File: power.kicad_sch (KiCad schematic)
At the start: 58 parts, among them Q1 AO3415A, SW2 SW_Push_Dual, U1 BQ25619RTWR, U2 TPS22917DBVR, U3 TPS63802DLAR, U4 MAX17260SEWL

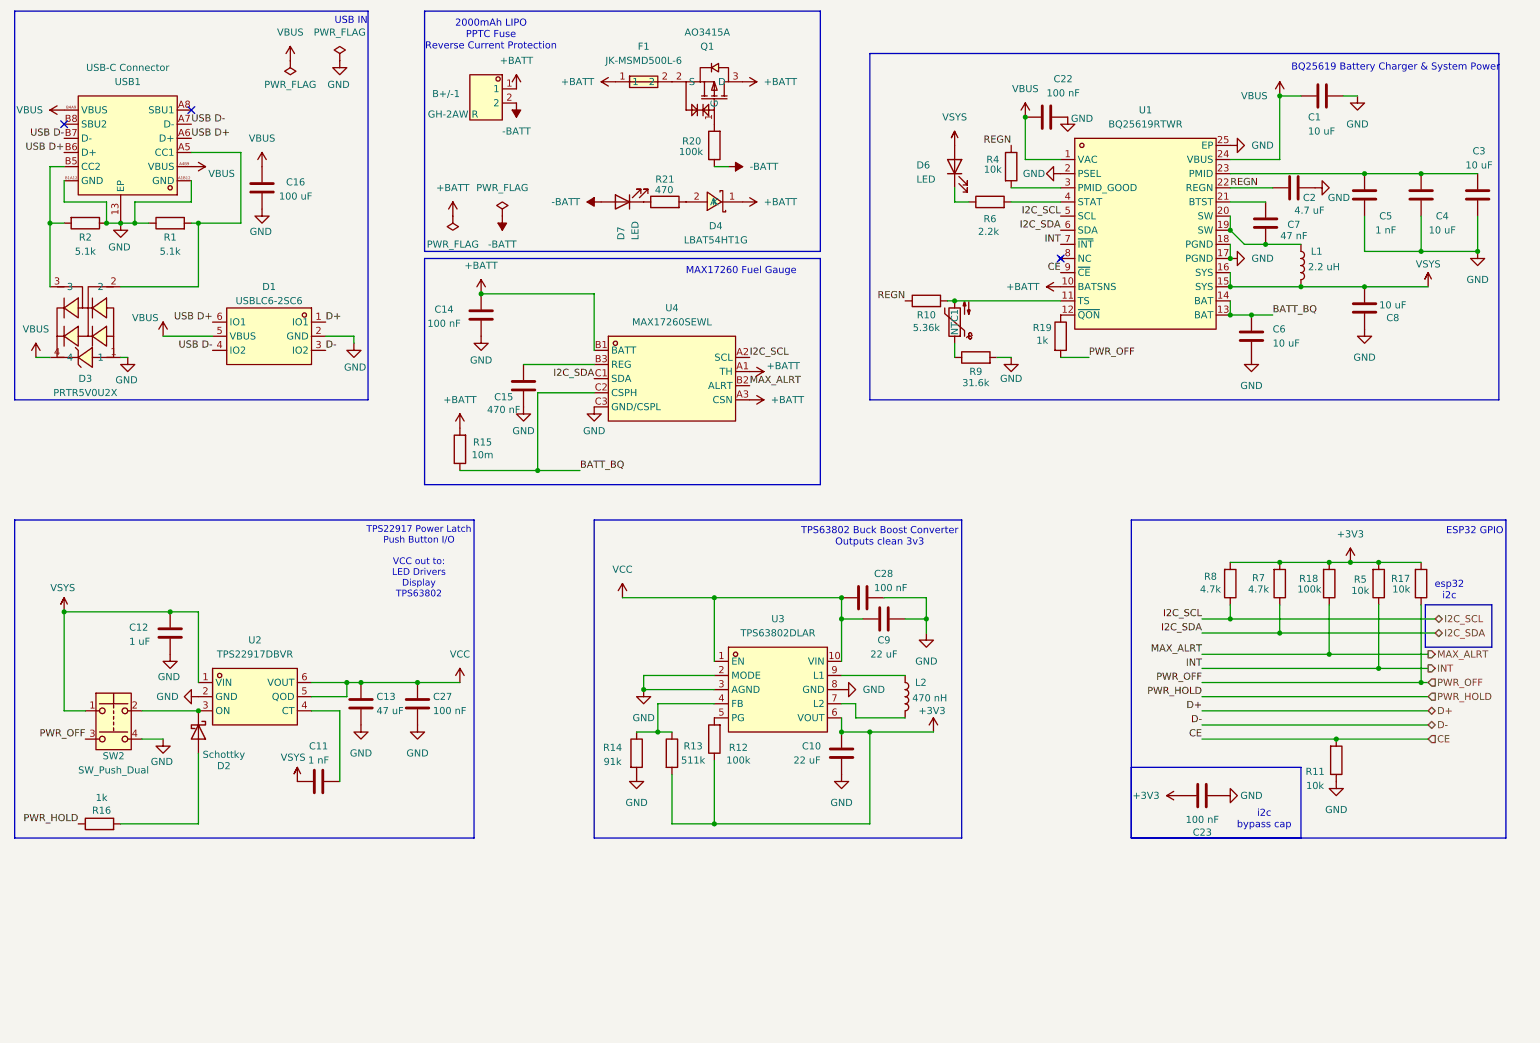
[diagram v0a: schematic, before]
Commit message: Add test points to schematic.
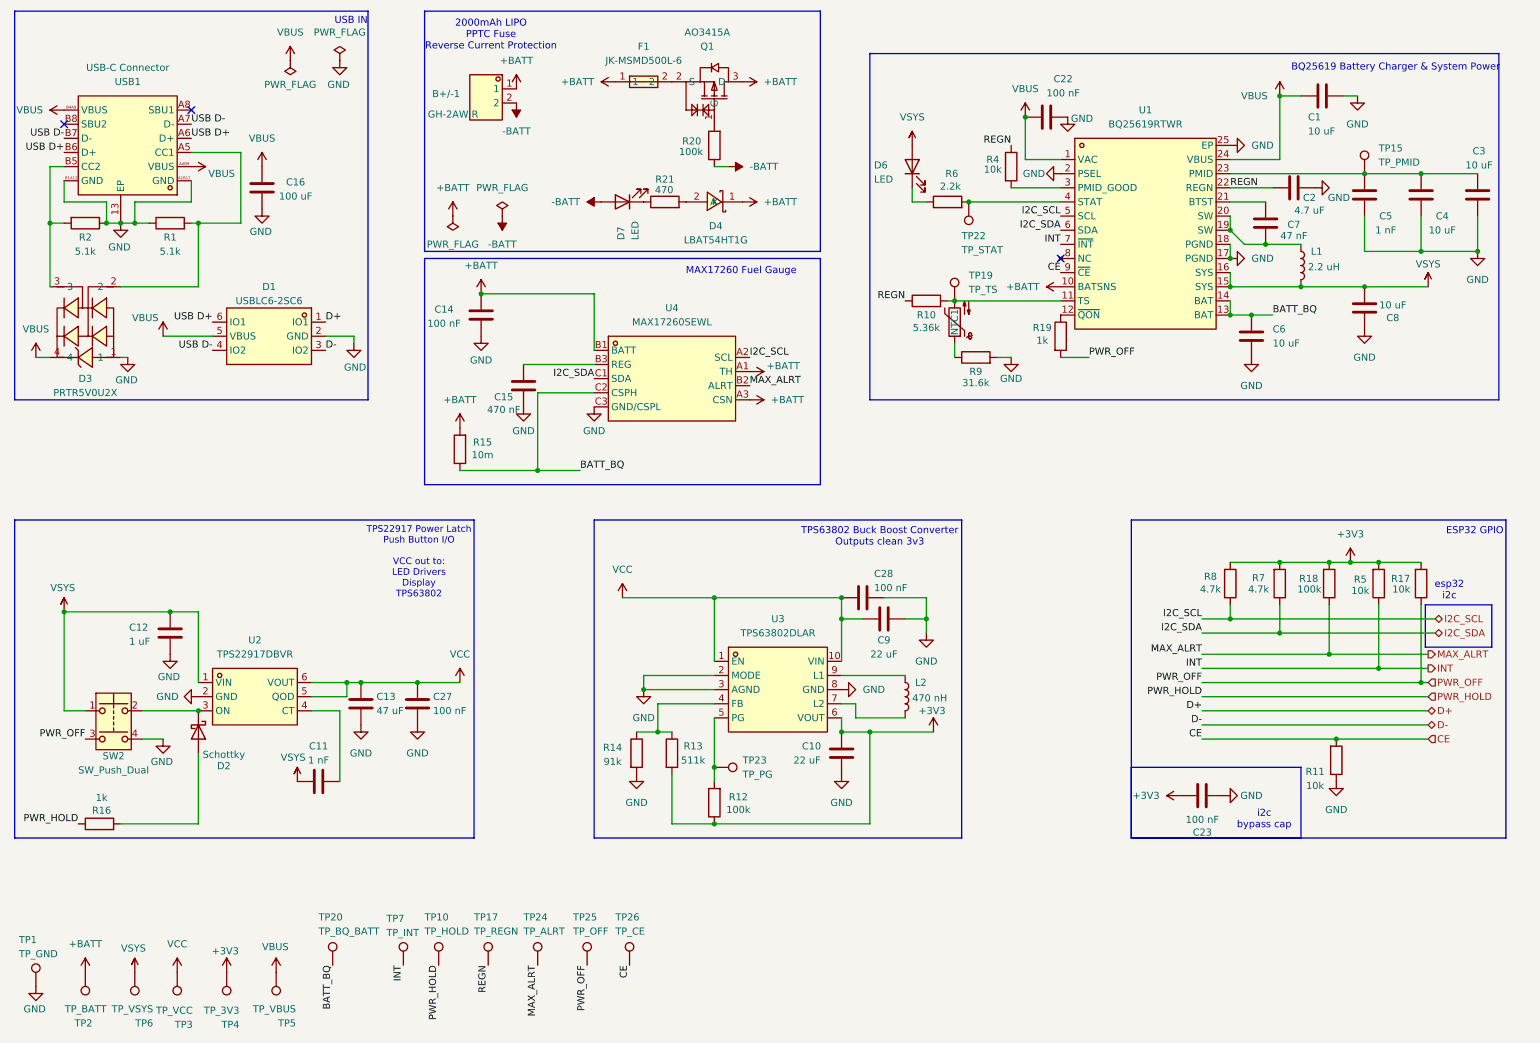
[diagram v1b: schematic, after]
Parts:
- added TP1: TP_GND, symbol Connector:TestPoint
- added TP10: TP_HOLD, symbol Connector:TestPoint
- added TP15: TP_PMID, symbol Connector:TestPoint
- added TP17: TP_REGN, symbol Connector:TestPoint
- added TP19: TP_TS, symbol Connector:TestPoint
- added TP2: TP_BATT, symbol Connector:TestPoint
- added TP20: TP_BQ_BATT, symbol Connector:TestPoint
- added TP22: TP_STAT, symbol Connector:TestPoint
- added TP23: TP_PG, symbol Connector:TestPoint
- added TP24: TP_ALRT, symbol Connector:TestPoint
- added TP25: TP_OFF, symbol Connector:TestPoint
- added TP26: TP_CE, symbol Connector:TestPoint
- added TP3: TP_VCC, symbol Connector:TestPoint
- added TP4: TP_3V3, symbol Connector:TestPoint
- added TP5: TP_VBUS, symbol Connector:TestPoint
- added TP6: TP_VSYS, symbol Connector:TestPoint
- added TP7: TP_INT, symbol Connector:TestPoint
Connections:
- net +3V3: now also TP4.1
- net +BATT: now also TP2.1
- net BATT_BQ: now also TP20.1
- net CE: now also TP26.1
- net GND: now also TP1.1
- net INT: now also TP7.1
- net MAX_ALRT: now also TP24.1
- net PWR_HOLD: now also TP10.1
- net PWR_OFF: now also TP25.1
- net REGN: now also TP17.1
- net VBUS: now also TP5.1
- net VCC: now also TP3.1
- net VSYS: now also TP6.1
- net at R12.2, U3.5 (PG): now also TP23.1
- net at R6.2, U1.4 (STAT): now also TP22.1
- net at NTC1.2, R10.2, U1.11 (TS): now also TP19.1
- net at C3.1, C4.1, C5.1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: now also TP15.1
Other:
- moved on the sheet: D6, R12, R6

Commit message: Add extracted data sheets to project.
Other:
- moved on the sheet: C1, C16, D1, D3, R1, R13, R14, TP10, TP17, TP20, TP23, TP24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

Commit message: Fix LED's -> anode wired to VCC, not GND.
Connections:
- net GND: now also R1.2, R2.2; no longer R1.1, R2.1
- net at D3.2, USB1.A5 (CC1): now also R1.1; no longer R1.2
- net at D3.3, USB1.B5 (CC2): now also R2.1; no longer R2.2
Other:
- moved on the sheet: C16, D1, D3, USB1
